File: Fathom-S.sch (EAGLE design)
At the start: 110 parts, among them IC1 LMH6643, IC2 LMH6643, IC3 ST490AB, IC4 ST490AB, IC5 FT230XS, Q1 BC817-40W, U1 MC7812, U2 MC7805, U4 INA139, U5 MC7805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

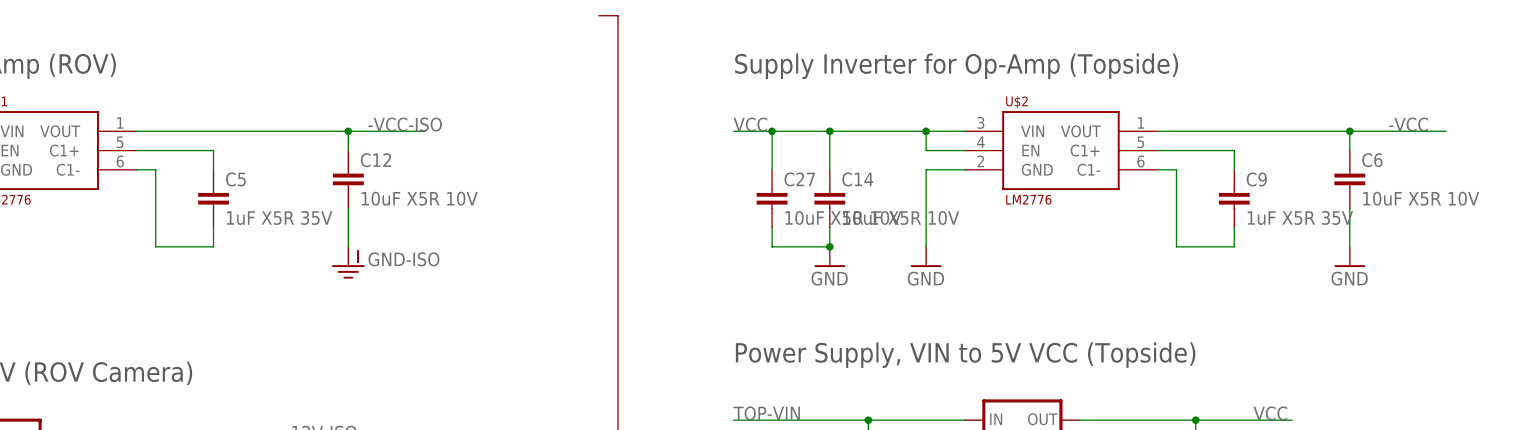
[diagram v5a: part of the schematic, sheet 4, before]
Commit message: Yet more layout changes and added ferrite beads to the -5V outputs for better noise rejection.
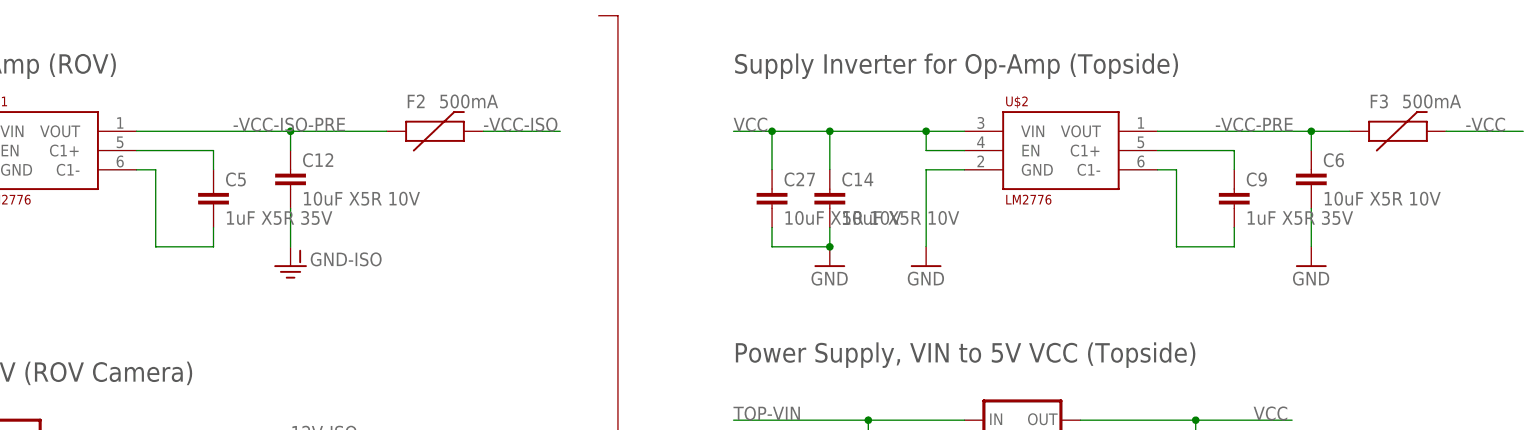
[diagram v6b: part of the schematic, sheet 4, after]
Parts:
- added F2, F3: 500mA, SparkFun:PTC0603
- U$5: value LOGOBR-LOGO-MS -> LOGOBR-LOGO-MS-COPPER; device BR-Eagle-Library:LOGOBR-LOGO-MS -> BlueRobotics-Main:LOGOBR-LOGO-MS-COPPER
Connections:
- new net -VCC-ISO-PRE: C12.1, F2.1, U$1.VOUT
- new net -VCC-PRE: C6.1, F3.1, U$2.VOUT
- net -VCC: now also F3.2; no longer C6.1, U$2.VOUT
- net -VCC-ISO: now also F2.2; no longer C12.1, U$1.VOUT
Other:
- moved on the sheet: C12, C6
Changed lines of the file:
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@@
 <part name="SJ2" library="SparkFun-Passives" deviceset="JUMPER-PAD-3-2OF3_NC_BY_PASTE" device="" value=""/>
 <part name="U$4" library="BlueRobotics-Main" deviceset="LOGO" device="FULL-M" value="LOGOFULL-M"/>
-<part name="U$5" library="BR-Eagle-Library" deviceset="LOGO" device="BR-LOGO-MS" value="LOGOBR-LOGO-MS"/>
+<part name="U$5" library="BlueRobotics-Main" deviceset="LOGO" device="BR-LOGO-MS-COPPER" value="LOGOBR-LOGO-MS-COPPER"/>
 <part name="JP15" library="SparkFun-Connectors" deviceset="M04" device="PTH" value="0.1&quot; HEADER"/>
 <part name="U4" library="SparkFun-AnalogIC" deviceset="INA139" device="" value="INA139"/>
@@
 <part name="C27" library="SparkFun-Passives" deviceset="CAP" device="0805" value="10uF X5R 10V"/>
 <part name="R18" library="SparkFun-Electromechanical" deviceset="TRIMPOT" device="-2" value="TC33X-2-102E"/>
+<part name="F2" library="SparkFun" deviceset="PTC" device="0603" value="500mA"/>
+<part name="F3" library="SparkFun" deviceset="PTC" device="0603" value="500mA"/>
 </parts>
 <sheets>
@@
 <instance part="GND-ISO13" gate="G$1" x="20.32" y="152.4"/>
 <instance part="GND-ISO14" gate="G$1" x="33.02" y="152.4"/>
-<instance part="GND-ISO15" gate="G$1" x="91.44" y="152.4"/>
+<instance part="GND-ISO15" gate="G$1" x="83.82" y="152.4"/>
 <instance part="U$2" gate="G$1" x="185.42" y="162.56"/>
 <instance part="C9" gate="G$1" x="208.28" y="160.02"/>
 <instance part="C14" gate="G$1" x="154.94" y="160.02"/>
 <instance part="GND12" gate="1" x="154.94" y="152.4"/>
-<instance part="GND13" gate="1" x="223.52" y="152.4"/>
+<instance part="GND13" gate="1" x="218.44" y="152.4"/>
 <instance part="GND17" gate="1" x="167.64" y="152.4"/>
 <instance part="C13" gate="G$1" x="76.2" y="121.92"/>
@@
 <instance part="GND-ISO28" gate="G$1" x="45.72" y="111.76"/>
 <instance part="U2" gate="G$1" x="180.34" y="132.08"/>
-<instance part="C6" gate="G$1" x="223.52" y="162.56"/>
-<instance part="C12" gate="G$1" x="91.44" y="162.56"/>
+<instance part="C6" gate="G$1" x="218.44" y="162.56"/>
+<instance part="C12" gate="G$1" x="83.82" y="162.56"/>
 <instance part="C26" gate="G$1" x="12.7" y="160.02"/>
 <instance part="C27" gate="G$1" x="147.32" y="160.02"/>
+<instance part="F2" gate="G$1" x="101.6" y="170.18" smashed="yes">
+<attribute name="NAME" x="99.06" y="173.228" size="1.778" layer="95"/>
+<attribute name="VALUE" x="103.378" y="173.228" size="1.778" layer="96"/>
+</instance>
+<instance part="F3" gate="G$1" x="228.6" y="170.18" smashed="yes">
+<attribute name="NAME" x="226.06" y="173.228" size="1.778" layer="95"/>
+<attribute name="VALUE" x="230.378" y="173.228" size="1.778" layer="96"/>
+</instance>
 </instances>
 <busses>
@@
 <pinref part="U$1" gate="G$1" pin="C1-"/>
 <wire x1="66.04" y1="165.1" x2="63.5" y2="165.1" width="0.1524" layer="91"/>
-</segment>
-</net>
-<net name="-VCC-ISO" class="0">
-<segment>
-<pinref part="U$1" gate="G$1" pin="VOUT"/>
-<wire x1="63.5" y1="170.18" x2="91.44" y2="170.18" width="0.1524" layer="91"/>
-<label x="93.98" y="170.18" size="1.778" layer="95"/>
-<wire x1="91.44" y1="170.18" x2="101.6" y2="170.18" width="0.1524" layer="91"/>
-<wire x1="91.44" y1="167.64" x2="91.44" y2="170.18" width="0.1524" layer="91"/>
-<junction x="91.44" y="170.18"/>
-<pinref part="C12" gate="G$1" pin="1"/>
 </segment>
 </net>
@@
 <segment>
 <pinref part="GND-ISO15" gate="G$1" pin="GND-ISO"/>
-<wire x1="91.44" y1="154.94" x2="91.44" y2="160.02" width="0.1524" layer="91"/>
+<wire x1="83.82" y1="154.94" x2="83.82" y2="160.02" width="0.1524" layer="91"/>
 <pinref part="C12" gate="G$1" pin="2"/>
 </segment>
@@
 <segment>
 <pinref part="GND13" gate="1" pin="GND"/>
-<wire x1="223.52" y1="154.94" x2="223.52" y2="160.02" width="0.1524" layer="91"/>
+<wire x1="218.44" y1="154.94" x2="218.44" y2="160.02" width="0.1524" layer="91"/>
 <pinref part="C6" gate="G$1" pin="2"/>
 </segment>
@@
 <pinref part="U$2" gate="G$1" pin="C1-"/>
 <wire x1="200.66" y1="165.1" x2="198.12" y2="165.1" width="0.1524" layer="91"/>
-</segment>
-</net>
-<net name="-VCC" class="0">
-<segment>
-<pinref part="U$2" gate="G$1" pin="VOUT"/>
-<wire x1="198.12" y1="170.18" x2="223.52" y2="170.18" width="0.1524" layer="91"/>
-<label x="228.6" y="170.18" size="1.778" layer="95"/>
-<wire x1="223.52" y1="170.18" x2="236.22" y2="170.18" width="0.1524" layer="91"/>
-<wire x1="223.52" y1="167.64" x2="223.52" y2="170.18" width="0.1524" layer="91"/>
-<junction x="223.52" y="170.18"/>
-<pinref part="C6" gate="G$1" pin="1"/>
 </segment>
 </net>
@@
 </segment>
 </net>
+<net name="-VCC-ISO" class="0">
+<segment>
+<pinref part="F2" gate="G$1" pin="2"/>
+<wire x1="109.22" y1="170.18" x2="119.38" y2="170.18" width="0.1524" layer="91"/>
+<label x="109.22" y="170.18" size="1.778" layer="95"/>
+</segment>
+</net>
+<net name="-VCC-ISO-PRE" class="0">
+<segment>
+<pinref part="U$1" gate="G$1" pin="VOUT"/>
+<wire x1="63.5" y1="170.18" x2="83.82" y2="170.18" width="0.1524" layer="91"/>
+<label x="76.2" y="170.18" size="1.778" layer="95"/>
+<wire x1="83.82" y1="170.18" x2="96.52" y2="170.18" width="0.1524" layer="91"/>
+<wire x1="83.82" y1="167.64" x2="83.82" y2="170.18" width="0.1524" layer="91"/>
+<junction x="83.82" y="170.18"/>
+<pinref part="C12" gate="G$1" pin="1"/>
+<pinref part="F2" gate="G$1" pin="1"/>
+</segment>
+</net>
+<net name="-VCC" class="0">
+<segment>
+<pinref part="F3" gate="G$1" pin="2"/>
+<wire x1="236.22" y1="170.18" x2="246.38" y2="170.18" width="0.1524" layer="91"/>
+<label x="238.76" y="170.18" size="1.778" layer="95"/>
+</segment>
+</net>
+<net name="-VCC-PRE" class="0">
+<segment>
+<pinref part="U$2" gate="G$1" pin="VOUT"/>
+<wire x1="198.12" y1="170.18" x2="218.44" y2="170.18" width="0.1524" layer="91"/>
+<label x="205.74" y="170.18" size="1.778" layer="95"/>
+<wire x1="218.44" y1="170.18" x2="223.52" y2="170.18" width="0.1524" layer="91"/>
+<wire x1="218.44" y1="167.64" x2="218.44" y2="170.18" width="0.1524" layer="91"/>
+<junction x="218.44" y="170.18"/>
+<pinref part="C6" gate="G$1" pin="1"/>
+<pinref part="F3" gate="G$1" pin="1"/>
+</segment>
+</net>

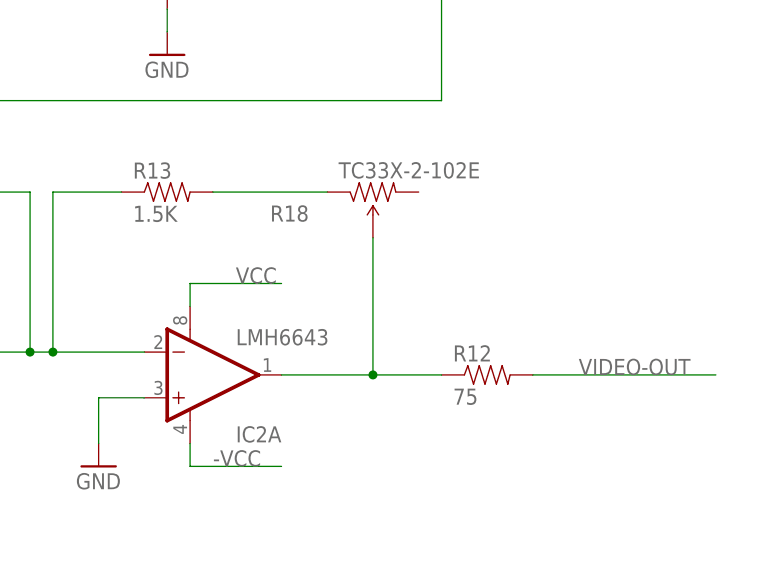
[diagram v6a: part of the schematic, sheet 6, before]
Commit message: Fixed a few more layout issues and connected the pot wiper to open end for safety.
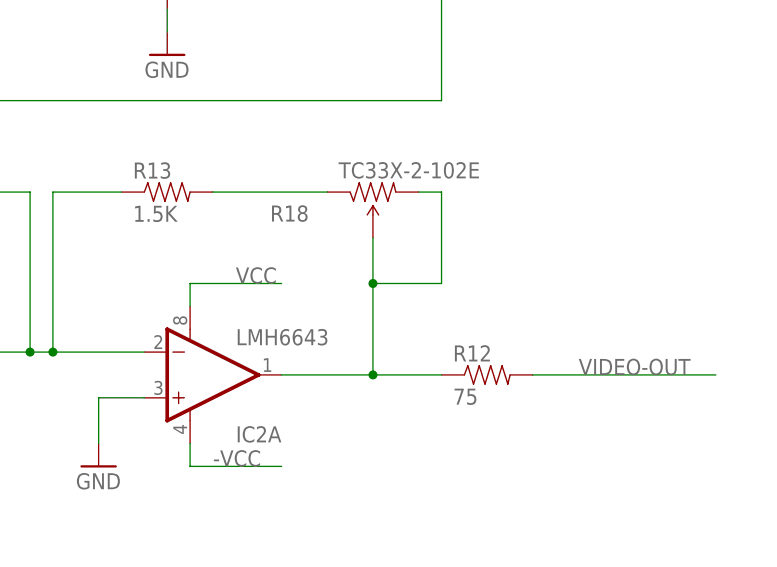
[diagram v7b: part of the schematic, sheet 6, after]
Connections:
- net N$17: now also R18.CW
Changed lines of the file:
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@@
 <pinref part="R18" gate="R?" pin="WIPER"/>
 <wire x1="203.2" y1="76.2" x2="193.04" y2="76.2" width="0.1524" layer="91"/>
-<wire x1="203.2" y1="91.44" x2="203.2" y2="76.2" width="0.1524" layer="91"/>
+<wire x1="203.2" y1="91.44" x2="203.2" y2="86.36" width="0.1524" layer="91"/>
 <junction x="203.2" y="76.2"/>
+<pinref part="R18" gate="R?" pin="CW"/>
+<wire x1="203.2" y1="86.36" x2="203.2" y2="76.2" width="0.1524" layer="91"/>
+<wire x1="208.28" y1="96.52" x2="210.82" y2="96.52" width="0.1524" layer="91"/>
+<wire x1="210.82" y1="96.52" x2="210.82" y2="86.36" width="0.1524" layer="91"/>
+<wire x1="210.82" y1="86.36" x2="203.2" y2="86.36" width="0.1524" layer="91"/>
+<junction x="203.2" y="86.36"/>
 </segment>
 </net>

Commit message: Change resistor value to fix RTS reset and added more thermal vias for regulators.
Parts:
- R17: value 10K -> 47K
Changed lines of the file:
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@@
 <part name="U$12" library="BR-Eagle-Library" deviceset="HEADER-2" device=""/>
 <part name="C11" library="SparkFun" deviceset="CAP" device="0603-CAP" value="1uF"/>
-<part name="R17" library="SparkFun" deviceset="RESISTOR" device="0603-RES" value="10K"/>
+<part name="R17" library="SparkFun" deviceset="RESISTOR" device="0603-RES" value="47K"/>
 <part name="SJ4" library="SparkFun-Passives" deviceset="JUMPER-PAD-2-NC_BY_PASTE" device=""/>
 <part name="C6" library="SparkFun-Passives" deviceset="CAP" device="0805" value="10uF X5R 10V"/>
